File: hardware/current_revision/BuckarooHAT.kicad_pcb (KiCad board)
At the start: 2 copper layers, 64.1 x 17 mm, 16 parts, among them J1 +12V PoE In, J2 Raspberry Pi Power In, J3 GEC03SBSN-M89, U1 AP62301WU

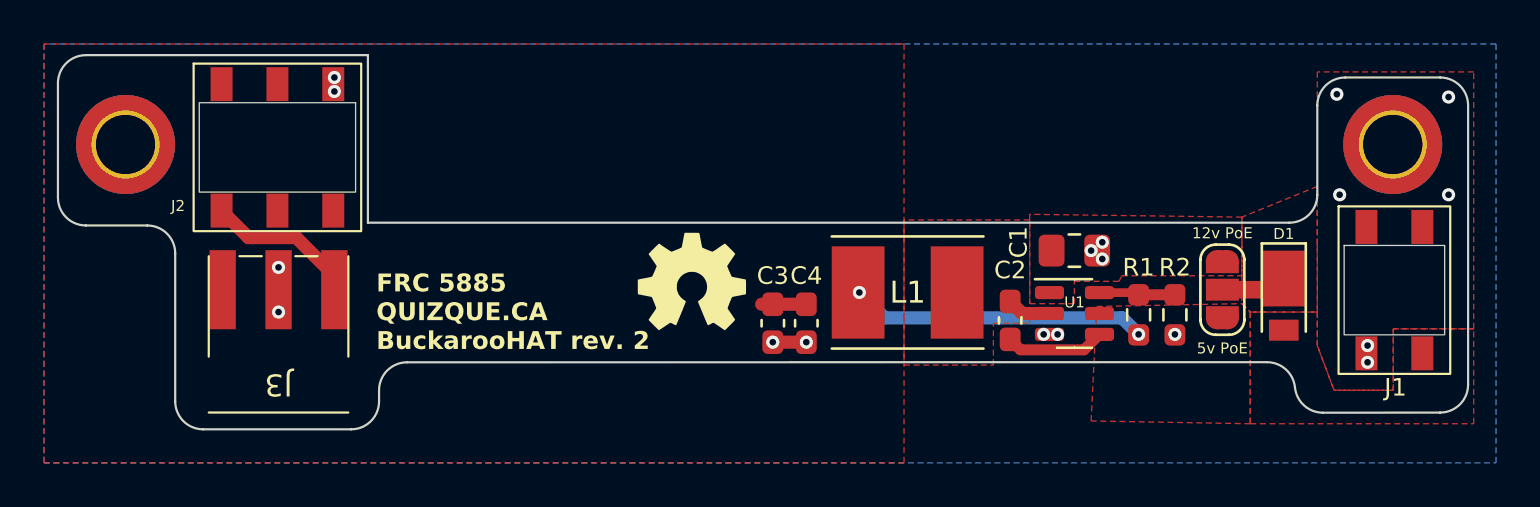
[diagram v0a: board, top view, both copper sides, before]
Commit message: Fixed footprint for buck
How did this happen???
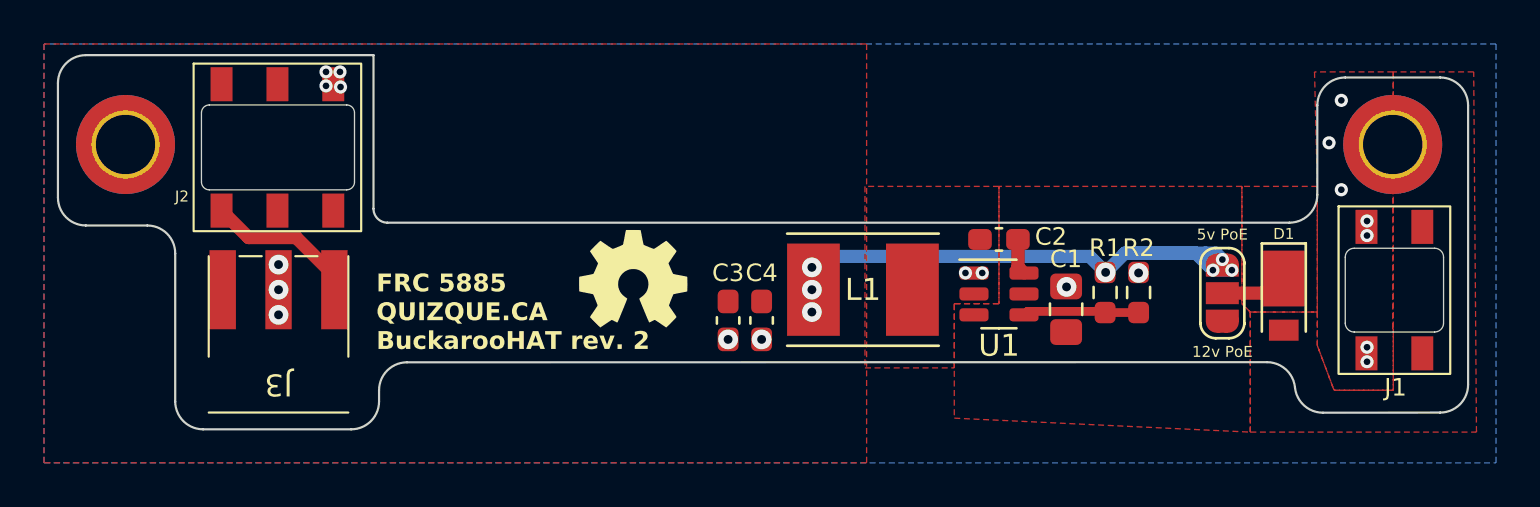
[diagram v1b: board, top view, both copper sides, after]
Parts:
- moved C2 3.72 mm to (141.4, 78.6), turned to 0 degrees
- moved U1 3.55 mm to (141.4, 81.1)
- moved C1 2.69 mm to (144.4, 81.8), turned to 90 degrees
- moved G*** 2.67 mm to (124.7, 80.4)
- moved L1 2.04 mm to (135.2, 80.9)
- moved C3 2.04 mm to (129.0, 82.3)
- moved C4 2.04 mm to (130.6, 82.3)
- moved R2 1.94 mm to (147.7, 81.0), turned to 90 degrees
- moved R1 1.83 mm to (146.2, 81.0), turned to -90 degrees
- moved JP1 0.16 mm to (151.5, 81.1), turned to -90 degrees
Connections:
- J1 pad 2: unconnected-(J1-Pin_2-Pad2) -> GND
- J1 pad 4: unconnected-(J1-Pin_4-Pad4) -> VCC
- U1 pad 1: /+12v -> GND
- U1 pad 3: GND -> /+12v
- U1 pad 4: Net-(U1-BST) -> /fb_in
- U1 pad 6: /fb_in -> Net-(U1-BST)
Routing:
- net +5V: track 15.0 -> 29.7 mm, vias 2 -> 7
- net Net-(U1-BST): track 4.55 -> 1.64 mm
- net /sw_out: track 2.02 -> 0.00 mm
- net /fb_in: track 3.47 -> 5.30 mm
- net GND: track 1.52 -> 0.00 mm, vias 18 -> 20
- net /vsplit: track 3.00 -> 3.79 mm
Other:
- outline, holes or cut-outs redrawn
